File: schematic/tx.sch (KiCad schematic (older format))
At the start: 33 parts, among them Q18 IRF4905, Q19 2N3904, Q20 2N3906, Q21 2N3904, Q22 RD15HVF1, Q23 2N3904, T5 FT37-43, T6 FT37-43

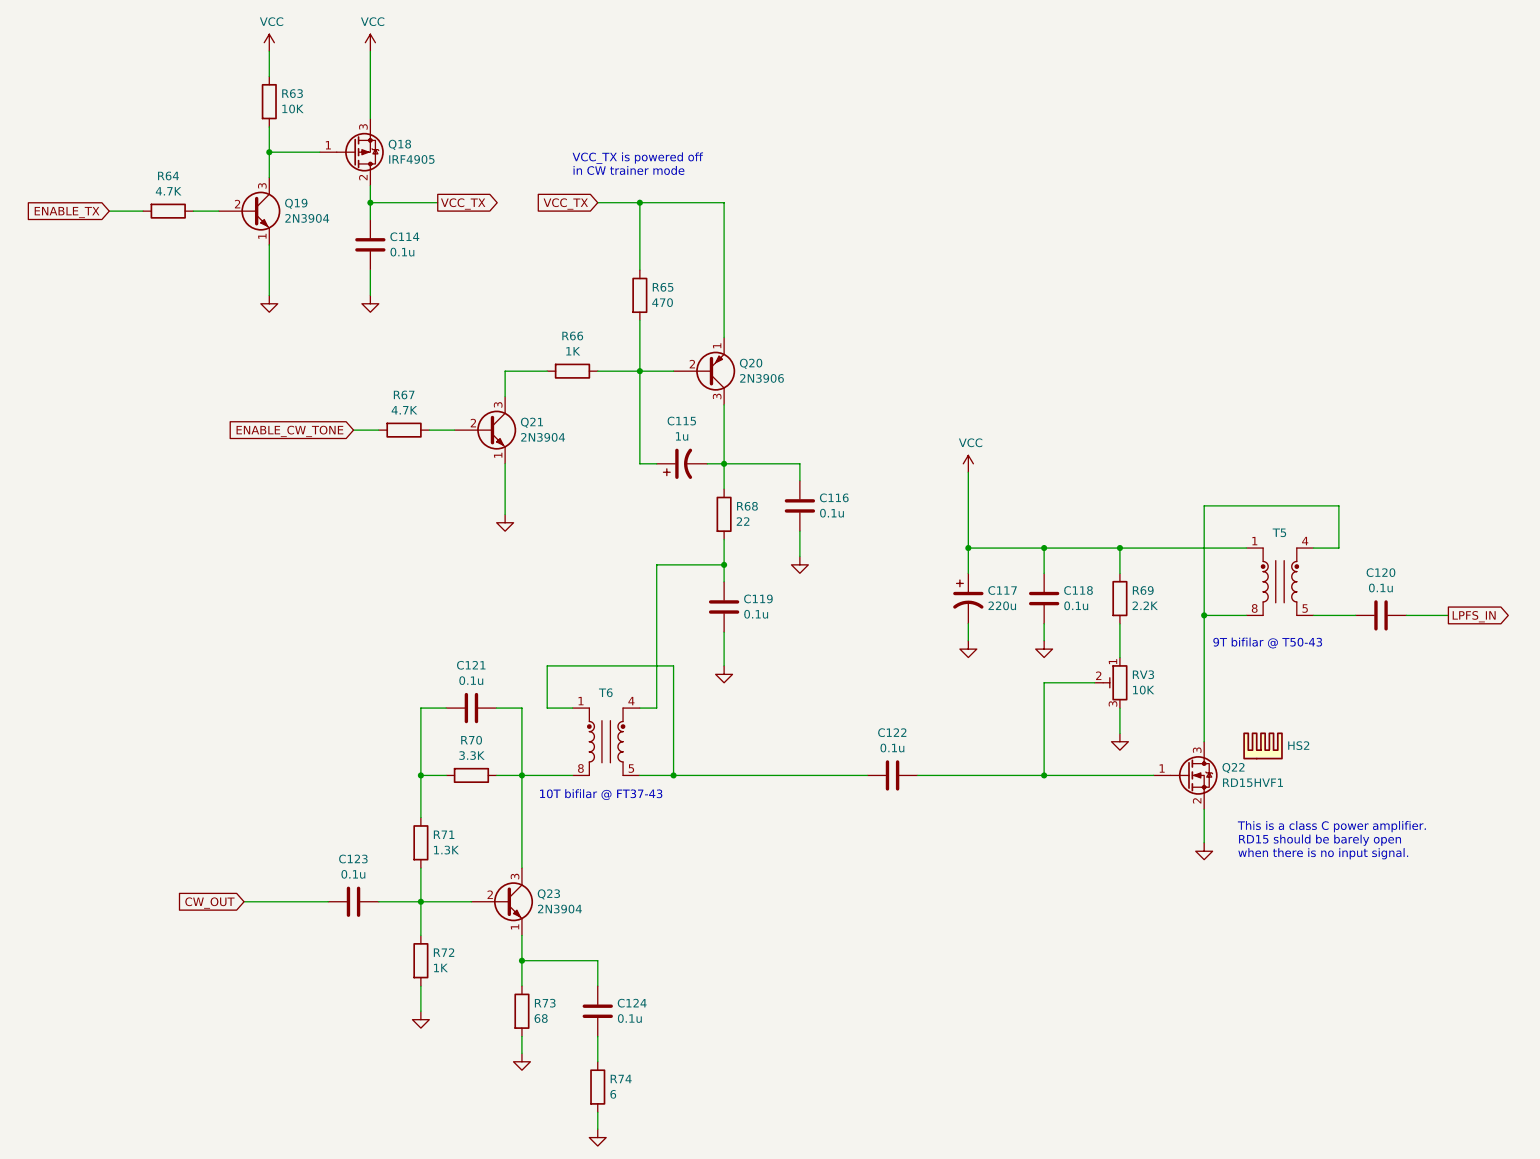
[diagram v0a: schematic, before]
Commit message: Correct the schematic
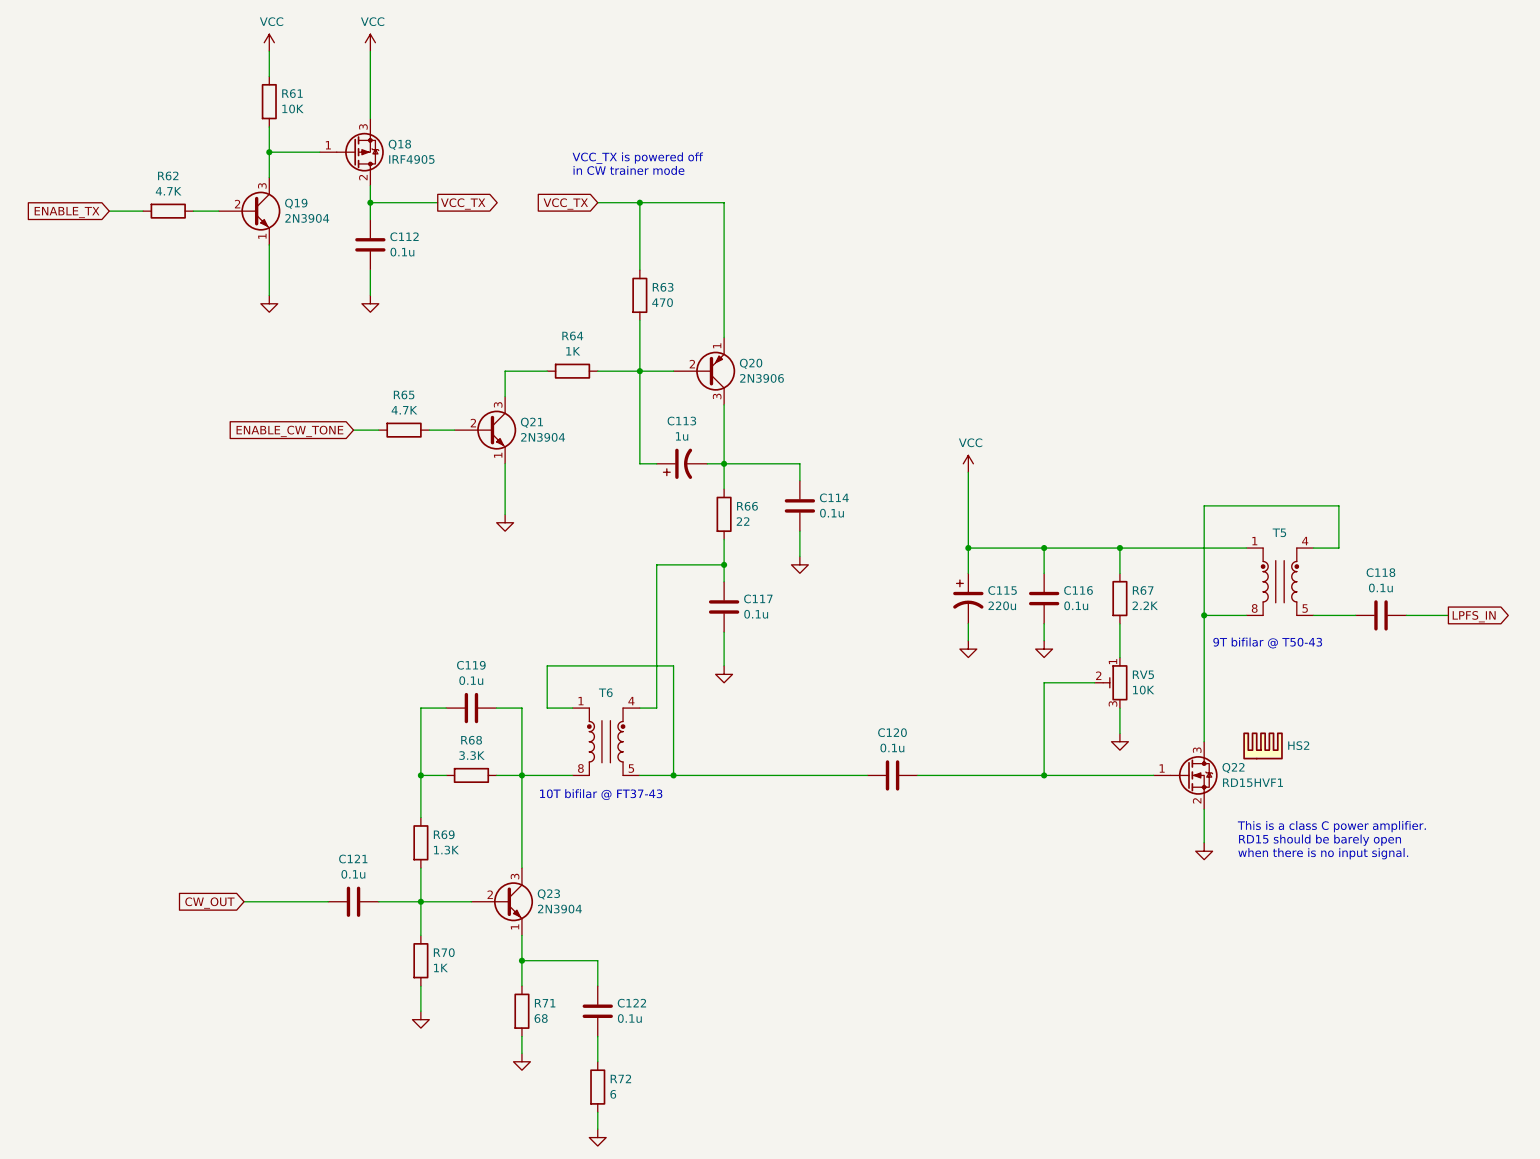
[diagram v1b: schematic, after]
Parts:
- renumbered C114 to C112, C115 to C113, C116 to C114, C117 to C115, C118 to C116, C119 to C117, C120 to C118, C121 to C119, C122 to C120, C123 to C121, C124 to C122, R63 to R61, R64 to R62, R65 to R63, R66 to R64, R67 to R65, R68 to R66, R69 to R67, R70 to R68, R71 to R69, R72 to R70, R73 to R71, R74 to R72, RV3 to RV5
